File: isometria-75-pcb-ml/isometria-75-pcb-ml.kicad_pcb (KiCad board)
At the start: 2 copper layers, 308.3 x 123 mm, 278 parts, among them J1 USB, J2 SWD, Q1 AO3400A, Q2 AO3401A, Q3 2N7002, SW1 Rotary_Encoder_Switch, U1 TXB0101, U2 XC6206P332MR, U3 nRF52840_holyiot_18010

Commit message: final checks
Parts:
- added C8: 100n, Capacitor_SMD:C_0603_1608Metric_Pad1.05x0.95mm_HandSolder, B.Cu at (139.7, 105.6)
- moved G*** 3.26 mm to (104.5, 100.0)
- renumbered C9 to C10, C10 to C11, C11 to C12, C12 to C13, C13 to C14, C14 to C15, C15 to C16, C16 to C17, C17 to C18, C18 to C19, C19 to C20, C20 to C21, C21 to C22, C22 to C23, C23 to C24, C24 to C25, C25 to C26, C26 to C27, C27 to C28, C8 to C9
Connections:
- J1 pad 5: chgsense -> VBUS
- U3 pad 22: +5V -> VBUS
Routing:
- net VBUS: track 0.00 -> 14.6 mm
- net +5V: track 2007.4 -> 1993.1 mm

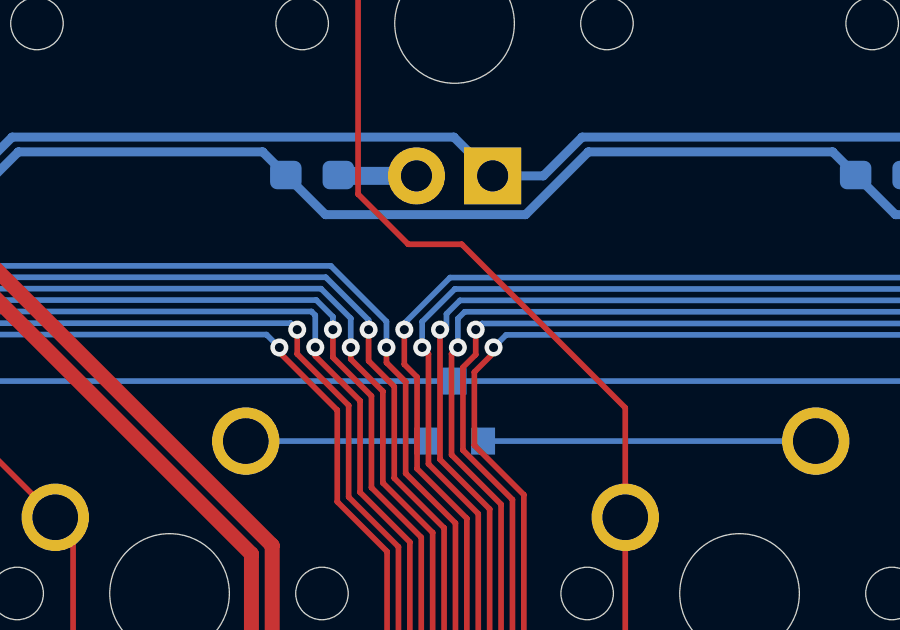
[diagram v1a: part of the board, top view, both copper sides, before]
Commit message: removed silkscreen labels from obvious components
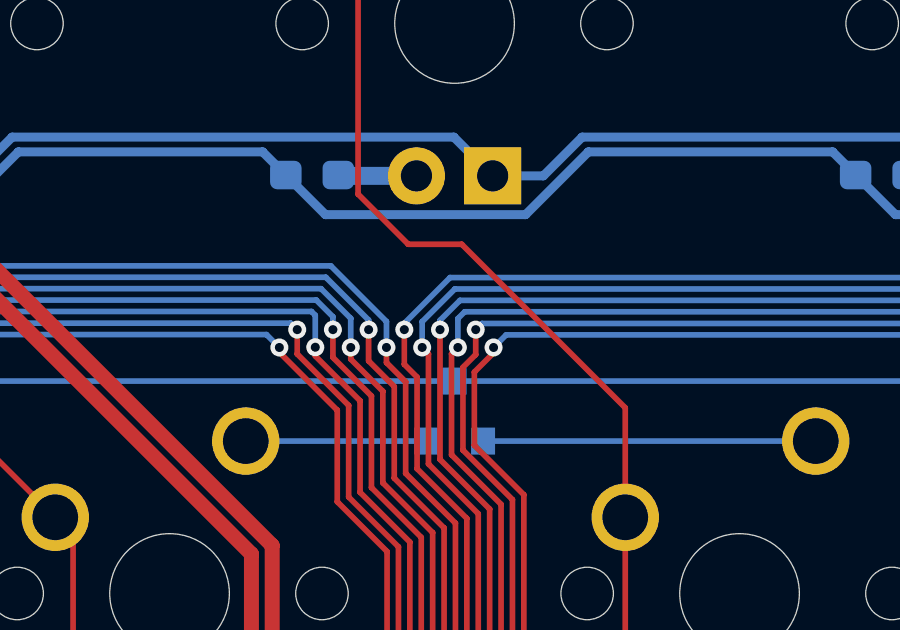
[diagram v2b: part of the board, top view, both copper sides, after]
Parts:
- D1, D10, D11, D12, D13, D14, D15, D16, D17, D18, D19, D2, D20, D21, D22, D23, D24, D25, D26, D27, D28, D29, D3, D30, D31, D32, D33, D34, D35, D36, D37, D38, D39, D4, D40, D41, D42, D43, D44, D45, D5, D6, D7, D8, D9: footprint Package_TO_SOT_SMD:SOT-23 -> kicad-keyboard-parts:SOT-23_stealth
- R10, R11, R12, R13, R14, R15, R16, R17, R18, R19, R20, R21, R22, R23, R25, R26, R27, R28, R29, R30, R31, R32, R33, R34, R35, R36, R37, R38, R39, R40, R41, R42, R43, R44, R45, R46, R47, R48, R49, R50, R51, R52, R53, R54, R55, R56, R57, R58, R59, R60, R61, R62, R63, R64, R65, R66, R67, R68, R69, R70, R71, R72, R73, R74, R75, R76, R77, R78, R79, R80, R81, R82, R83, R84, R85, R86, R87, R88, R89, R90, R91, R92, R93: footprint Resistor_SMD:R_0603_1608Metric_Pad1.05x0.95mm_HandSolder -> kicad-keyboard-parts:R_0603_1608Metric_stealth_HandSolder
